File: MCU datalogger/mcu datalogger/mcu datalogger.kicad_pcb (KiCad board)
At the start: 2 copper layers, 29 parts, among them J1 Conn_01x04_Pin, J2 Conn_01x09_Pin, J3 Conn_01x04_Pin, J4 Conn_02x03_Odd_Even, U1 24LC1025, U2 DS1337S_, U3 24LC1025, U4 ATMEGA328P-AU, Y1 32.768 KHz, Y2 16MHz

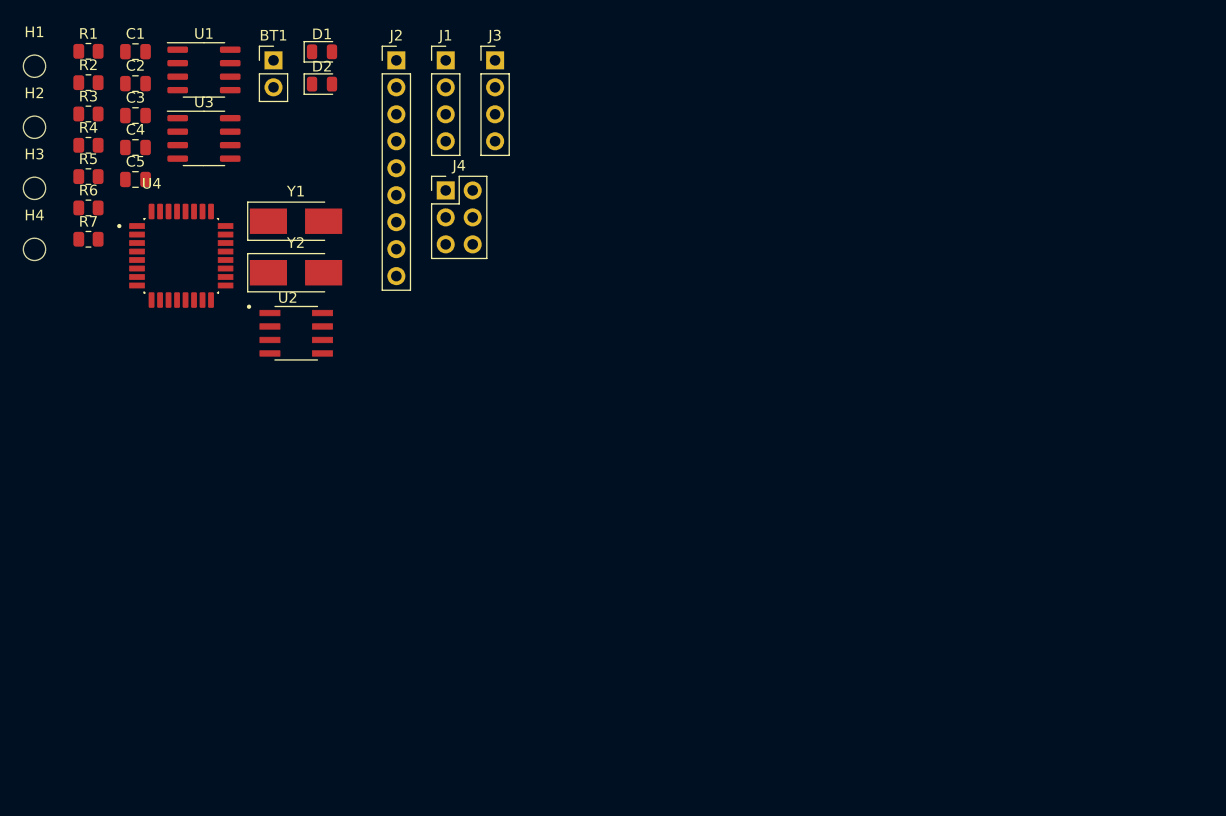
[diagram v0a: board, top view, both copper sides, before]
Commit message: Completed the footprints placement.
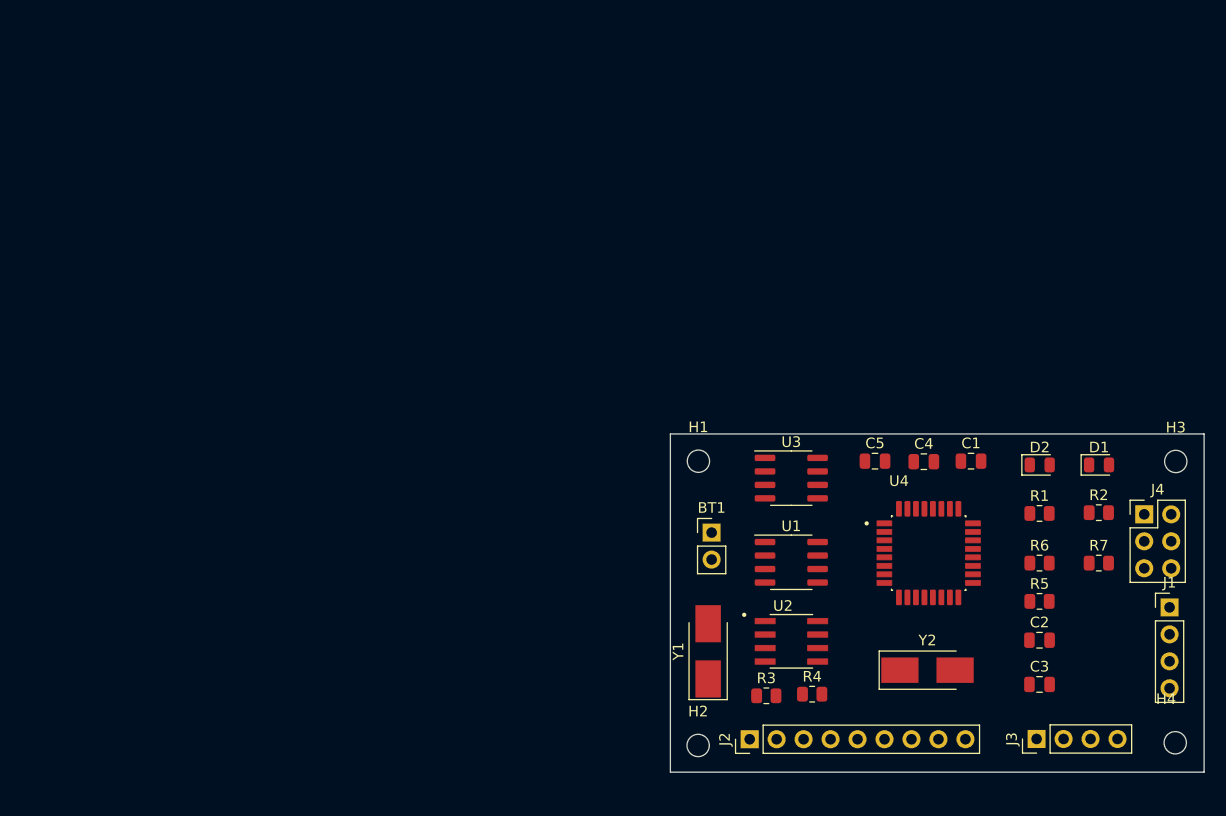
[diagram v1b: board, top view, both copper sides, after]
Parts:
- moved H4 117.1 mm to (149.9, 95.2)
- moved H3 110.5 mm to (149.9, 68.7)
- moved R2 103.4 mm to (142.7, 73.5)
- moved C3 100.6 mm to (137.1, 89.7)
- moved C2 100.0 mm to (137.1, 85.5)
- moved R7 99.9 mm to (142.7, 78.3)
- moved R1 99.6 mm to (137.1, 73.6)
- moved R5 98.1 mm to (137.1, 81.9)
- moved R6 95.6 mm to (137.1, 78.3)
- moved C1 87.6 mm to (130.6, 68.7)
- moved R4 85.5 mm to (115.7, 90.6)
- moved J1 85.5 mm to (149.3, 82.4)
- moved H2 85.4 mm to (104.9, 95.5)
- moved R3 84.1 mm to (111.3, 90.8)
- moved D1 82.9 mm to (142.7, 69.0)
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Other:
- board outline added: 50.3 x 31.9 mm

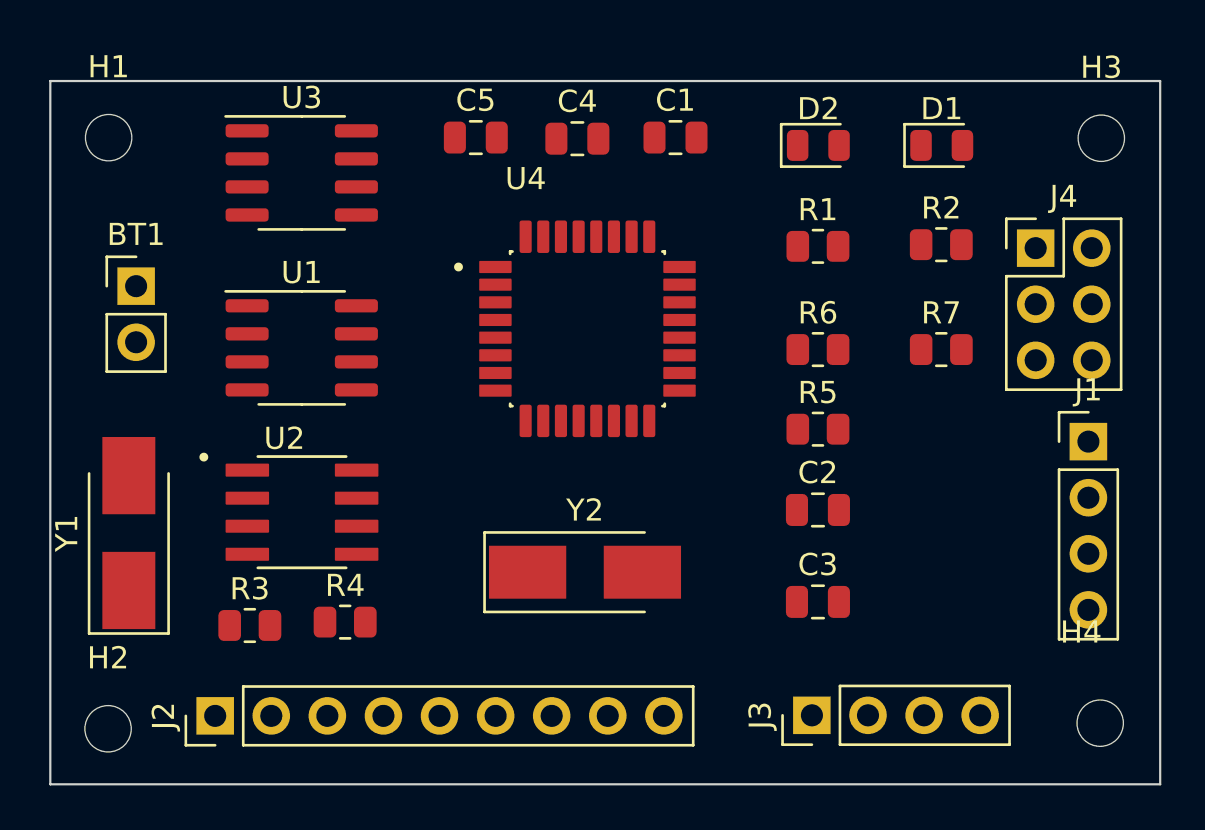
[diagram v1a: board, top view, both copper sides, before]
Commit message: Done routing the tracks.
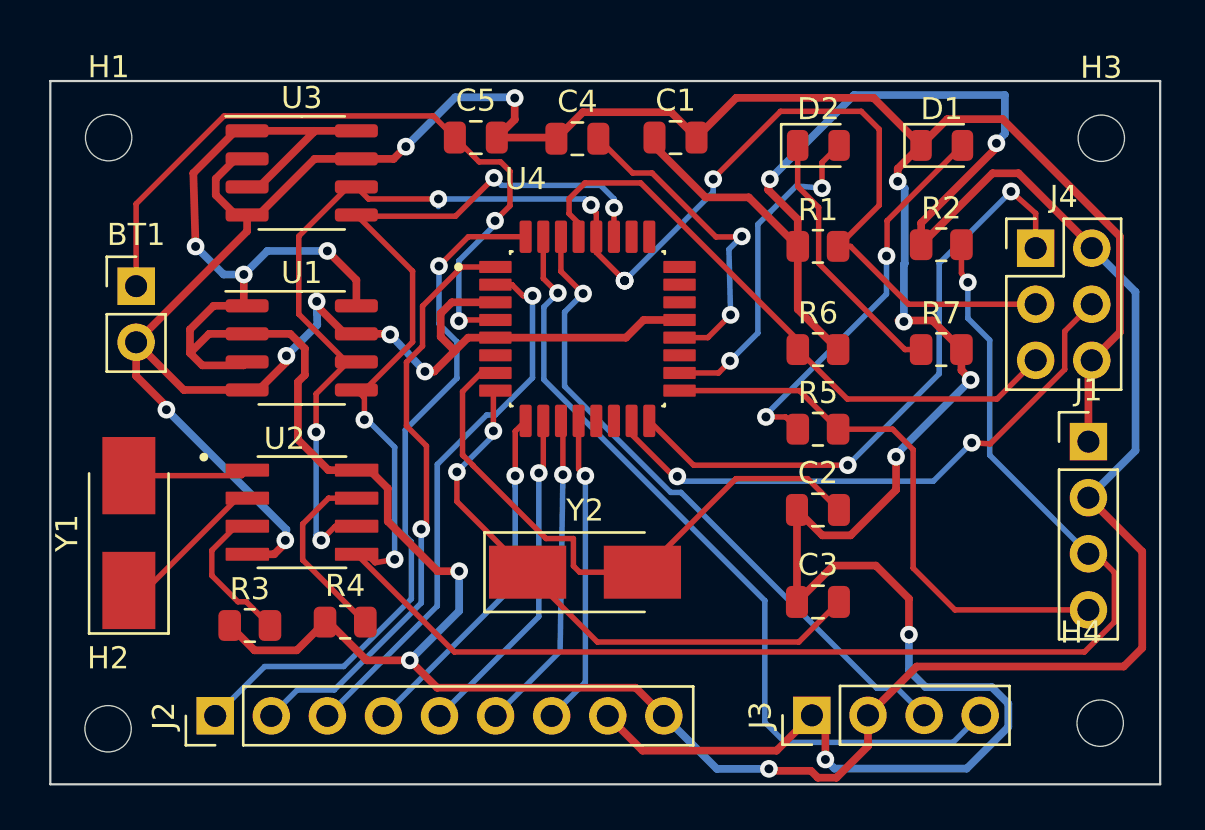
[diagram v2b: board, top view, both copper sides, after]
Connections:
- R5 pad 2: /SCK -> /SCL
- U4 pad 17: /SCK -> /SCL
- U4 pad 28: /SCK -> /SCL
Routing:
- net GND: track 0.00 -> 190.1 mm, vias 0 -> 14
- net /Vcc: track 0.00 -> 178.9 mm, vias 0 -> 8
- net /SCL: track 0.00 -> 96.2 mm, vias 0 -> 7
- net /SDA: track 0.00 -> 92.5 mm, vias 0 -> 5
- net Net-(BT1-+): track 0.00 -> 48.3 mm, vias 0 -> 4
- net /TX: track 0.00 -> 37.3 mm, vias 0 -> 1
- net /D2: track 0.00 -> 32.0 mm, vias 0 -> 1
- net /RX: track 0.00 -> 30.0 mm, vias 0 -> 1
- net /MISO: track 0.00 -> 28.6 mm, vias 0 -> 2
- net /RST: track 0.00 -> 28.4 mm
- net Net-(U4-PB6): track 0.00 -> 27.0 mm
- net /MOSI: track 0.00 -> 26.9 mm, vias 0 -> 2
- net /D3: track 0.00 -> 26.8 mm, vias 0 -> 1
- net Net-(U4-PB7): track 0.00 -> 26.5 mm, vias 0 -> 2
- net /D4: track 0.00 -> 25.0 mm, vias 0 -> 1
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
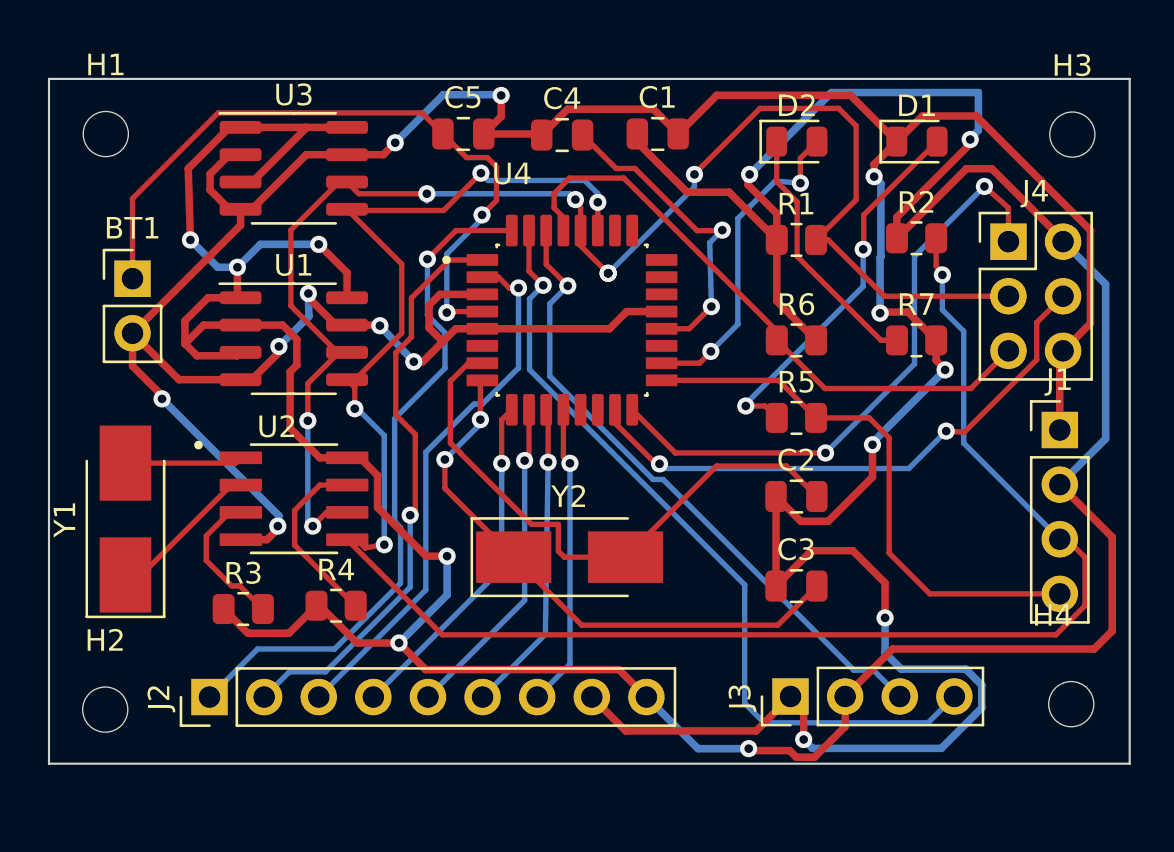
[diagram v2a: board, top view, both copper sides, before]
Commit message: Completed routing and copper filling.
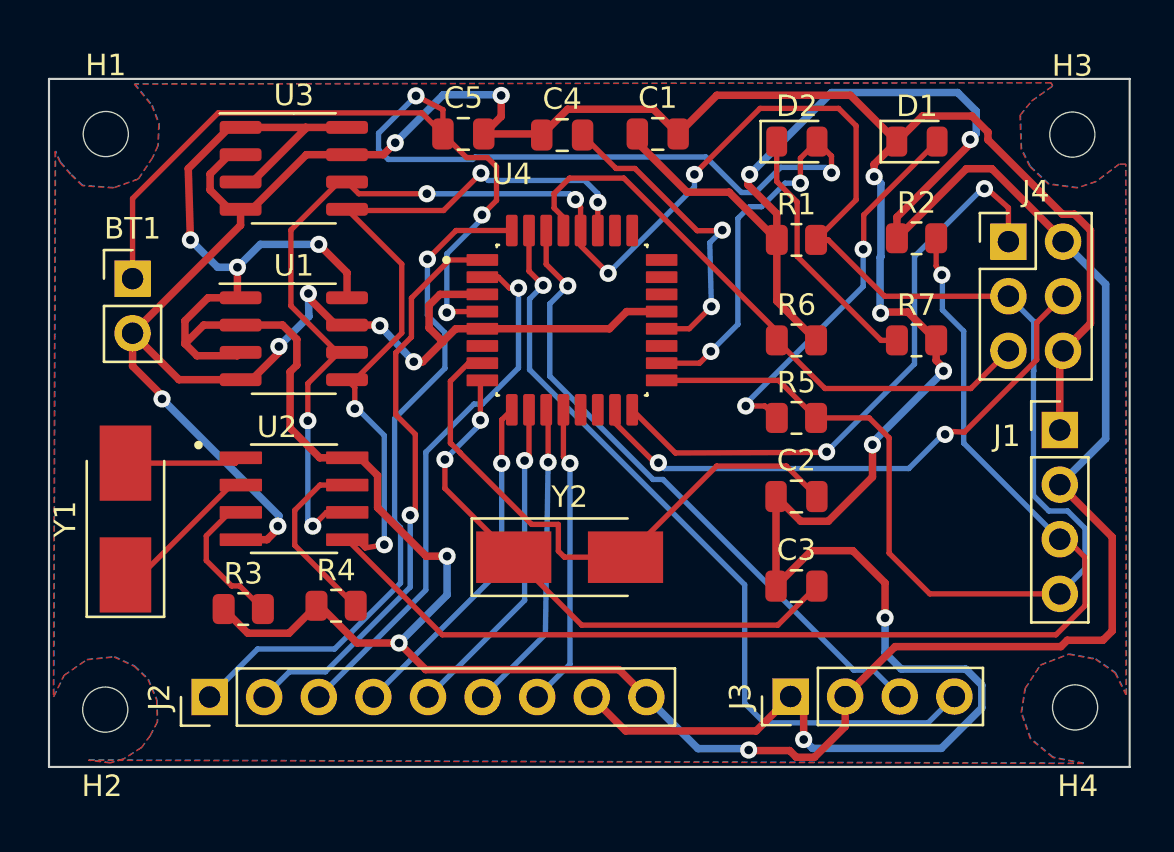
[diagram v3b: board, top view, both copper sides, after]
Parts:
- moved H4 0.23 mm to (150.0, 95.4)
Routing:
- net Net-(BT1-+): track 48.3 -> 77.5 mm, vias 4 -> 6
- net /SCL: track 96.2 -> 109.8 mm, vias 7 -> 6
- net /Vcc: track 178.9 -> 178.0 mm
- added copper zone on F.Cu, net /Vcc
- added copper zone on B.Cu, net GND
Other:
- board size 50.3 x 31.9 mm -> 50.3 x 32 mm

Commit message: Fixed outstanding issues.
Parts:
- added REF**: KiCad-Logo2_5mm_SilkScreen, Symbol:KiCad-Logo2_5mm_SilkScreen, B.Cu at (114.9, 70.2)
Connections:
- BT1 pad 1: Net-(BT1-+) -> /Vcc
- C5 pad 1: Net-(BT1-+) -> /Vcc
- D2 pad 2: Net-(BT1-+) -> /Vcc
- U4 pad 18: Net-(BT1-+) -> /Vcc
- U4 pad 4: Net-(BT1-+) -> /Vcc
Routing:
- net Net-(BT1-+): track 77.5 -> 0.00 mm, vias 6 -> 0
- net /Vcc: track 178.0 -> 244.8 mm, vias 8 -> 14
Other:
- board text added: "1"
- board text added: "2"
- board text added: "2MB EEPROM -RTC -I2C, SPI, GPIOs"
- board text added: "3"
- board text added: "4"
- board text added: "5"
- board text added: "6"
- board text added: "7"
- board text added: "Data logger with ATmega328p."
- board text added: "GND"
- board text added: "GPIO"
- board text added: "I2C"
- board text added: "ICSP"
- board text added: "ICSP MISO Vcc SCL MOSI RST GND"
- board text added: "RX"
- board text added: "SCL"
- board text added: "SDA"
- board text added: "SERIAL UART"
- board text added: "TX"
- board text added: "Vcc"

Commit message: Completed 2 layer PCB project.
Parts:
- removed REF**: KiCad-Logo2_5mm_SilkScreen, Symbol:KiCad-Logo2_5mm_SilkScreen
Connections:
- J4 pad 3: /SCL -> /SCK
- R5 pad 2: /SCL -> /SCK
- U4 pad 17: /SCL -> /SCK
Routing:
- net /SCL: track 109.8 -> 79.7 mm, vias 6 -> 8
- net /SCK: track 0.00 -> 27.7 mm, vias 0 -> 2
- net Net-(D1-A): track 17.5 -> 18.3 mm
- net Net-(D2-K): track 12.0 -> 12.7 mm

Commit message: Completed 2layer MCU Datalogger PCB.
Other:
- board text added: "BOARD CHARACTISTICS :"
- board text added: "Copper layer count : 2 Board Overall dimension : 32.3 mm x 50.47 mm Min track/spacing : 0.2000 mm / 0.0000 mm Copper finish : None Castellated pads : No"
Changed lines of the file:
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@@
     (pad "2" smd rect (at 2.6 0) (size 3.5 2.4) (layers "F.Cu" "F.Paste" "F.Mask")
       (net 3 "Net-(U4-PB6)") (pinfunction "2") (pintype "passive"))
-    (model "${KICAD6_3DMODEL_DIR}/Crystal.3dshapes/Crystal_SMD_5032-2Pin_5.0x3.2mm_HandSoldering.wrl"
+    (model ":KICAD7_3DMODEL_DIR:Crystal.3dshapes/Crystal_SMD_0603-4Pin_6.0x3.5mm.wrl"
       (offset (xyz 0 0 0))
       (scale (xyz 1 1 1))
@@
     (pad "32" smd roundrect (at -2.8 -4.17) (size 0.55 1.47) (layers "F.Cu" "F.Paste" "F.Mask") (roundrect_rratio 0.18)
       (net 10 "/D2") (pinfunction "PD2") (pintype "bidirectional") (solder_mask_margin 0.102))
+    (model ":KICAD7_3DMODEL_DIR:Package_QFP.3dshapes/TQFP-32_7x7mm_P0.8mm.step"
+      (offset (xyz 0 0 0))
+      (scale (xyz 1 1 1))
+      (rotate (xyz 0 0 0))
+    )
   )
   (footprint "Capacitor_SMD:C_0805_2012Metric" (layer "F.Cu")
@@
     (pad "8" smd roundrect (at 2.475 -1.905) (size 1.97 0.59) (layers "F.Cu" "F.Paste" "F.Mask") (roundrect_rratio 0.07)
       (net 2 "/Vcc") (pinfunction "VCC") (pintype "power_in") (solder_mask_margin 0.102))
+    (model ":KICAD7_3DMODEL_DIR:Package_SO.3dshapes/SO-8_3.9x4.9mm_P1.27mm.wrl"
+      (offset (xyz 0 0 0))
+      (scale (xyz 1 1 1))
+      (rotate (xyz 0 0 0))
+    )
   )
   (footprint "Resistor_SMD:R_0805_2012Metric" (layer "F.Cu")
@@
     (pad "2" smd rect (at 2.6 0 90) (size 3.5 2.4) (layers "F.Cu" "F.Paste" "F.Mask")
       (net 24 "Net-(U2-X1)") (pinfunction "2") (pintype "passive"))
-    (model "${KICAD6_3DMODEL_DIR}/Crystal.3dshapes/Crystal_SMD_5032-2Pin_5.0x3.2mm_HandSoldering.wrl"
+    (model ":KICAD7_3DMODEL_DIR:Crystal.3dshapes/Crystal_SMD_0603-4Pin_6.0x3.5mm.wrl"
       (offset (xyz 0 0 0))
       (scale (xyz 1 1 1))
@@
     (effects (font (size 0.8 0.8) (thickness 0.15)) (justify left bottom))
   )
+  (gr_text "Copper layer count : 2\n\nBoard Overall dimension : 32.3 mm x 50.47 mm\n\nMin track/spacing : 0.2000 mm / 0.0000 mm\n\nCopper finish : None\n\nCastellated pads : No" (at 177.165 87.3252) (layer "Edge.Cuts")
+    (effects (font (size 1 1) (thickness 0.15)) (justify left bottom))
+  )
+  (gr_text "BOARD CHARACTISTICS :" (at 176.6824 70.485) (layer "Edge.Cuts")
+    (effects (font (size 1.5 2) (thickness 0.375) bold) (justify left bottom))
+  )
+  (dimension (type aligned) (layer "Edge.Cuts")
+    (pts (xy 102.1334 102.616) (xy 152.6032 102.6414))
+    (height 2.911578)
+    (gr_text "50.4698 mm" (at 127.367414 104.390278 359.9711647) (layer "Edge.Cuts")
+      (effects (font (size 1 1) (thickness 0.15)))
+    )
+    (format (prefix "") (suffix "") (units 3) (units_format 1) (precision 4))
+    (style (thickness 0.1) (arrow_length 1.27) (text_position_mode 0) (extension_height 0.58642) (extension_offset 0.5) keep_text_aligned)
+  )
+  (dimension (type aligned) (layer "Edge.Cuts")
+    (pts (xy 96.2914 98.2472) (xy 96.266 65.9384))
+    (height 0.184088)
+    (gr_text "32.3088 mm" (at 97.612788 82.091751 -89.95495616) (layer "Edge.Cuts")
+      (effects (font (size 1 1) (thickness 0.15)))
+    )
+    (format (prefix "") (suffix "") (units 3) (units_format 1) (precision 4))
+    (style (thickness 0.1) (arrow_length 1.27) (text_position_mode 0) (extension_height 0.58642) (extension_offset 0.5) keep_text_aligned)
+  )
   (segment (start 111.2232 80.1072) (end 111.741373 80.1072) (width 0.35) (layer "F.Cu") (net 1))
